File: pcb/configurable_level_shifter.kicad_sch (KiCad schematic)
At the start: 4 parts, among them Q6 BSS138

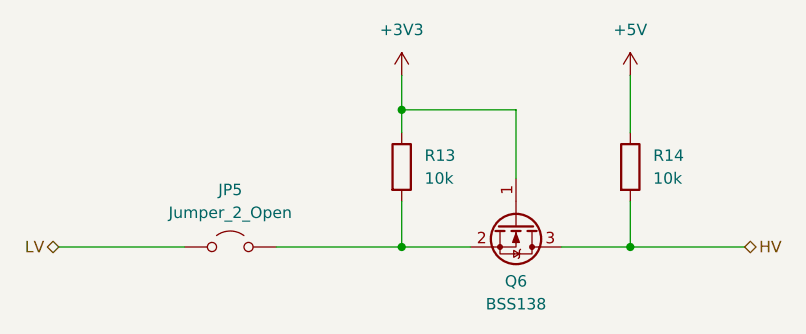
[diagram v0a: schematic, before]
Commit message: Convert PCB to KiCad 9.0 format
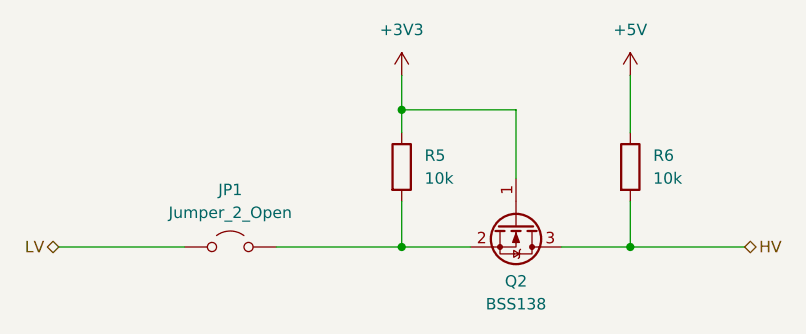
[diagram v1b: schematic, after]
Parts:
- renumbered JP5 to JP1, Q6 to Q2, R13 to R5, R14 to R6
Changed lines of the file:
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@@
 (kicad_sch
-	(version 20231120)
+	(version 20250114)
 	(generator "eeschema")
-	(generator_version "8.0")
+	(generator_version "9.0")
 	(paper "A4")
 	(junction
@@
 		(shape bidirectional)
 		(at 63.5 76.2 180)
-		(fields_autoplaced yes)
 		(effects
 			(font
@@
 		(shape bidirectional)
 		(at 139.7 76.2 0)
-		(fields_autoplaced yes)
 		(effects
 			(font
@@
 		(dnp no)
 		(fields_autoplaced yes)
-		(property "Reference" "R13"
+		(property "Reference" "R5"
 			(at 104.14 66.0399 0)
 			(effects
@@
 		(dnp no)
 		(fields_autoplaced yes)
-		(property "Reference" "#PWR063"
+		(property "Reference" "#PWR047"
 			(at 127 60.96 0)
 			(effects
@@
 		(dnp no)
 		(fields_autoplaced yes)
-		(property "Reference" "R14"
+		(property "Reference" "R6"
 			(at 129.54 66.0399 0)
 			(effects
@@
 		(dnp no)
 		(fields_autoplaced yes)
-		(property "Reference" "Q6"
+		(property "Reference" "Q2"
 			(at 114.3 80.01 90)
 			(effects
@@
 		(dnp no)
 		(fields_autoplaced yes)
-		(property "Reference" "#PWR061"
+		(property "Reference" "#PWR045"
 			(at 101.6 60.96 0)
 			(effects
@@
 		(dnp no)
 		(fields_autoplaced yes)
-		(property "Reference" "JP5"
+		(property "Reference" "JP1"
 			(at 82.55 69.85 0)
 			(effects
